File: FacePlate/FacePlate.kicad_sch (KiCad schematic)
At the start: 36 parts, among them J1 Conn_01x02_Pin, J2 GPIO, J3 Conn_01x04_Pin, J4 Conn_01x02_Pin, U7 AMS1117-3.3

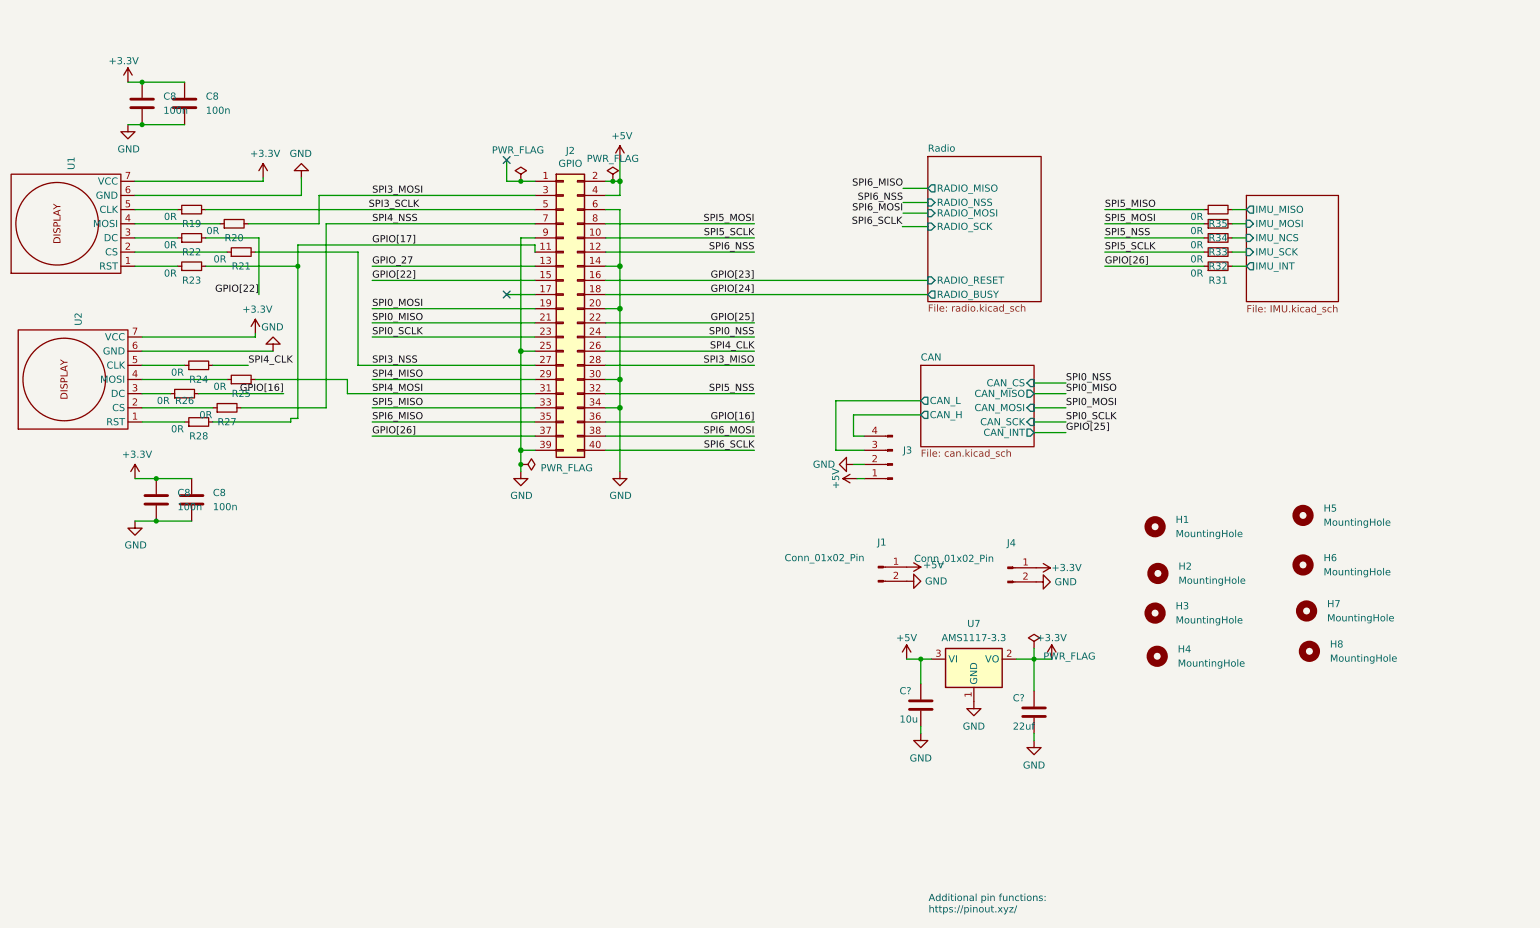
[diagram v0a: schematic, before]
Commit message: changed transceiver for faceplate
+ removed caps on chicker can
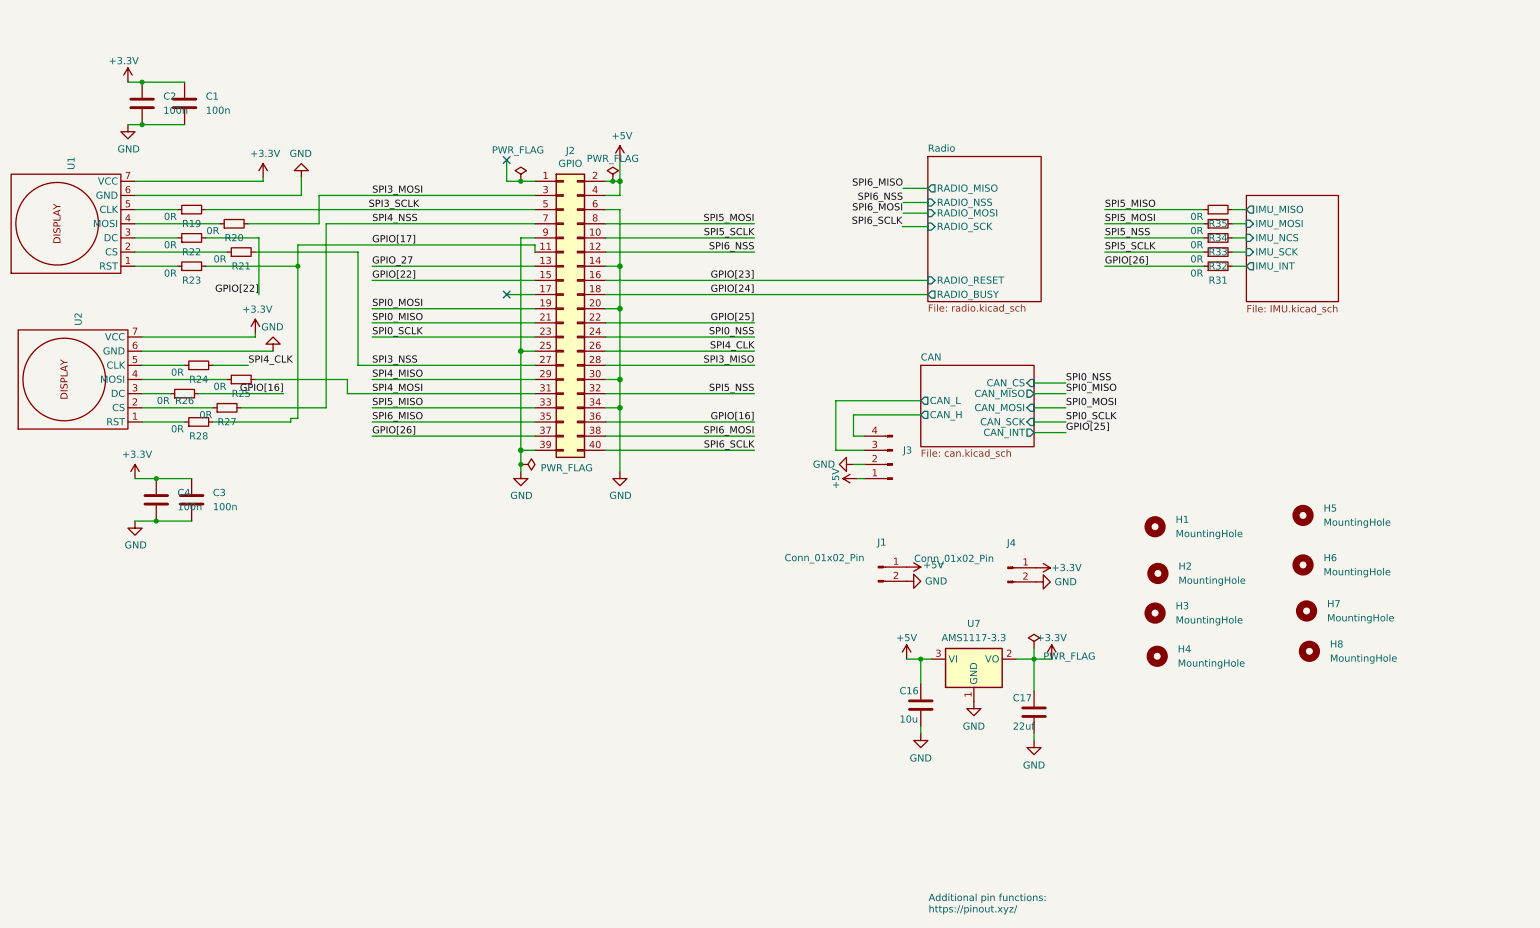
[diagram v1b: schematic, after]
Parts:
- gave numbers to parts that had none: 2
- renumbered C8 to C1, C8 to C2, C8 to C3, C8 to C4

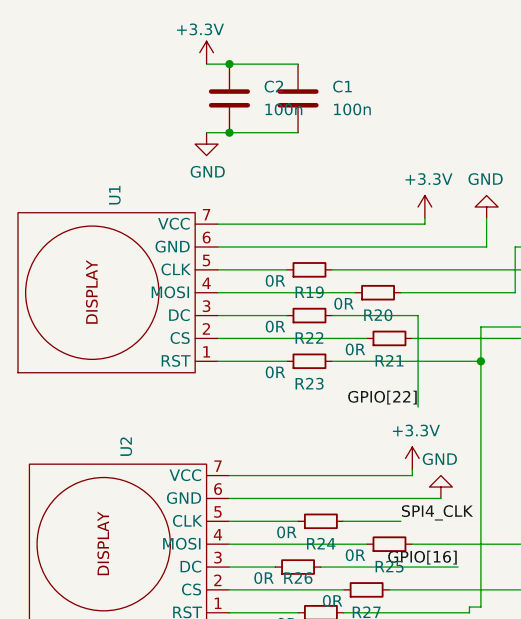
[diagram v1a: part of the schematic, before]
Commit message: faceplate. broken.
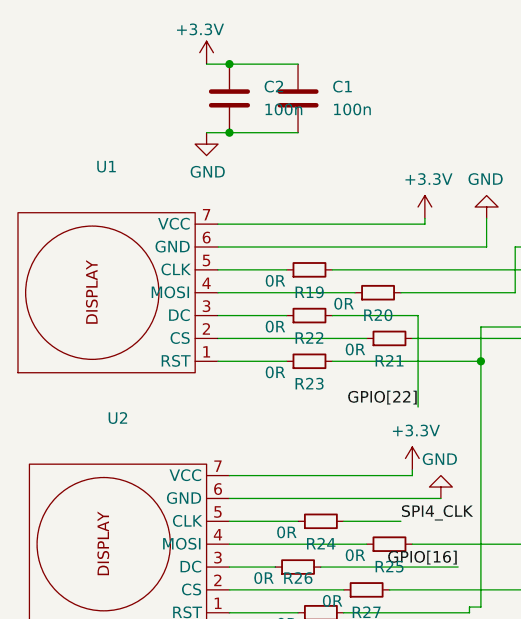
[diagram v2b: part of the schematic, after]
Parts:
- J2: footprint Connector_PinSocket_2.54mm:PinSocket_2x20_P2.54mm_Horizontal -> bots:PinSocket_2x20_P2.54mm_Horizontal; symbol Connector_Generic:Conn_02x20_Odd_Even -> bots:Conn_02x20_Odd_Even
- U1, U2: footprint Connector_PinSocket_2.54mm:PinSocket_1x07_P2.54mm_Vertical -> bots:GC9A_Display; symbol gc9a01:240_240_Round_Display -> bots:240_240_Round_Display
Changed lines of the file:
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@@
 	)
 	(symbol
-		(lib_id "Connector_Generic:Conn_02x20_Odd_Even")
+		(lib_id "bots:Conn_02x20_Odd_Even")
 		(at 113.665 71.12 0)
 		(unit 1)
@@
 			)
 		)
-		(property "Footprint" "Connector_PinSocket_2.54mm:PinSocket_2x20_P2.54mm_Horizontal"
-			(at -9.525 95.25 0)
+		(property "Footprint" "bots:PinSocket_2x20_P2.54mm_Horizontal"
+			(at 113.665 71.12 0)
 			(effects
 				(font
@@
 		)
 		(property "Datasheet" "~"
-			(at -9.525 95.25 0)
+			(at 113.665 71.12 0)
 			(effects
 				(font
@@
 			)
 		)
-		(property "Description" ""
+		(property "Description" "Generic connector, double row, 02x20, odd/even pin numbering scheme (row 1 odd numbers, row 2 even numbers), script generated (kicad-library-utils/schlib/autogen/connector/)"
 			(at 113.665 71.12 0)
 			(effects
@@
 					(size 1.27 1.27)
 				)
+				(hide yes)
 			)
 		)
@@
 	)
 	(symbol
-		(lib_id "gc9a01:240_240_Round_Display")
+		(lib_id "bots:240_240_Round_Display")
 		(at 12.7 83.82 90)
 		(unit 1)
@@
 		(fields_autoplaced yes)
 		(property "Reference" "U2"
-			(at 26.67 74.168 0)
+			(at 25.7175 69.85 90)
 			(effects
 				(font
 					(size 1.27 1.27)
 				)
-				(justify left)
 			)
 		)
 		(property "Value" "~"
-			(at 12.7 83.82 0)
+			(at 25.7175 72.39 90)
 			(effects
 				(font
@@
 			)
 		)
-		(property "Footprint" "Connector_PinSocket_2.54mm:PinSocket_1x07_P2.54mm_Vertical"
+		(property "Footprint" "bots:GC9A_Display"
 			(at 12.7 83.82 0)
 			(effects
@@
 					(size 1.27 1.27)
 				)
+				(hide yes)
 			)
 		)
@@
 	)
 	(symbol
-		(lib_id "gc9a01:240_240_Round_Display")
+		(lib_id "bots:240_240_Round_Display")
 		(at 11.43 55.88 90)
 		(unit 1)
@@
 		(fields_autoplaced yes)
 		(property "Reference" "U1"
-			(at 25.4 46.228 0)
+			(at 24.4475 41.91 90)
 			(effects
 				(font
 					(size 1.27 1.27)
 				)
-				(justify left)
 			)
 		)
 		(property "Value" "~"
-			(at 11.43 55.88 0)
+			(at 24.4475 44.45 90)
 			(effects
 				(font
@@
 			)
 		)
-		(property "Footprint" "Connector_PinSocket_2.54mm:PinSocket_1x07_P2.54mm_Vertical"
+		(property "Footprint" "bots:GC9A_Display"
 			(at 11.43 55.88 0)
 			(effects
@@
 					(size 1.27 1.27)
 				)
+				(hide yes)
 			)
 		)

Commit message: faceplate global files working
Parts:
- C16: footprint bots:C_0603_1608Metric -> bots:C_0805_2012Metric; symbol Device:C -> bots:C_10u; JLC (none) -> 0805; JLC Extended (none) -> no; LCSC C96446 -> C440198; MPN (none) -> GRM21BR61H106KE43L; Manufacturer (none) -> Murata; Price (none) -> 0.0645
- J3: symbol Connector:Conn_01x04_Pin -> bots:JST_XH_A_1x4
- R19, R20, R21, R22, R23, R24, R25, R26, R27, R28, R31, R32, R33, R34, R35: symbol bots:0R -> bots:R_0R; JLC (none) -> 0603; JLC Extended (none) -> no; MPN (none) -> 0603WAF0000T5E; Manufacturer (none) -> UNI-ROYAL(Uniroyal Elec); Price (none) -> 0.001
- U7: footprint Package_TO_SOT_SMD:SOT-223-3_TabPin2 -> bots:SOT-223-3_TabPin2; symbol Regulator_Linear:AMS1117-3.3 -> bots:AMS1117-3.3; JLC (none) -> SOT-223; JLC Extended (none) -> no; MPN (none) -> AMS1117-3.3; Manufacturer (none) -> Advanced Monolithic Systems; Price (none) -> 0.179
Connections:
- net GPIO[26]: no longer R31.1
- net IMU/IMU_INT: no longer R31.2
- net IMU/IMU_MISO: no longer R35.2
- net IMU/IMU_MOSI: no longer R34.2
- net IMU/IMU_NCS: no longer R33.2
- net IMU/IMU_SCK: no longer R32.2
- net SPI5_MISO: no longer R35.1
- net SPI5_MOSI: no longer R34.1
- net SPI5_NSS: no longer R33.1
- net SPI5_SCLK: no longer R32.1
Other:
- moved on the sheet: C16, C17, R19, R20, R22, R23, R24, R25, R27, R28

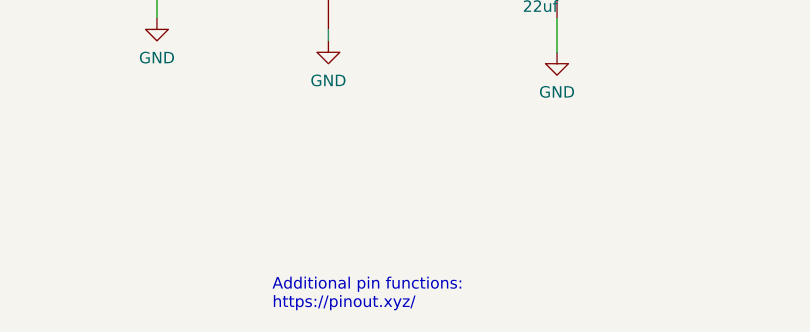
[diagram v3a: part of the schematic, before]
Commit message: added a title block
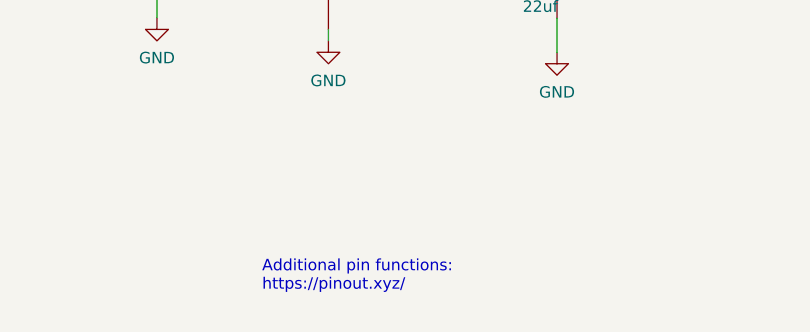
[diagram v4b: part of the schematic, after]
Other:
- company: (none) -> The Bots
- title: (none) -> Faceplate
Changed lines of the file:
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@@
 	(paper "A4")
 	(title_block
-		(date "15 nov 2012")
+		(title "Faceplate")
+		(date "2024-02-04")
+		(rev "V1.0")
+		(company "The Bots")
 	)
 	(text "Additional pin functions:\nhttps://pinout.xyz/"
 		(exclude_from_sim no)
-		(at 179.197 179.832 0)
+		(at 178.054 177.8 0)
 		(effects
 			(font

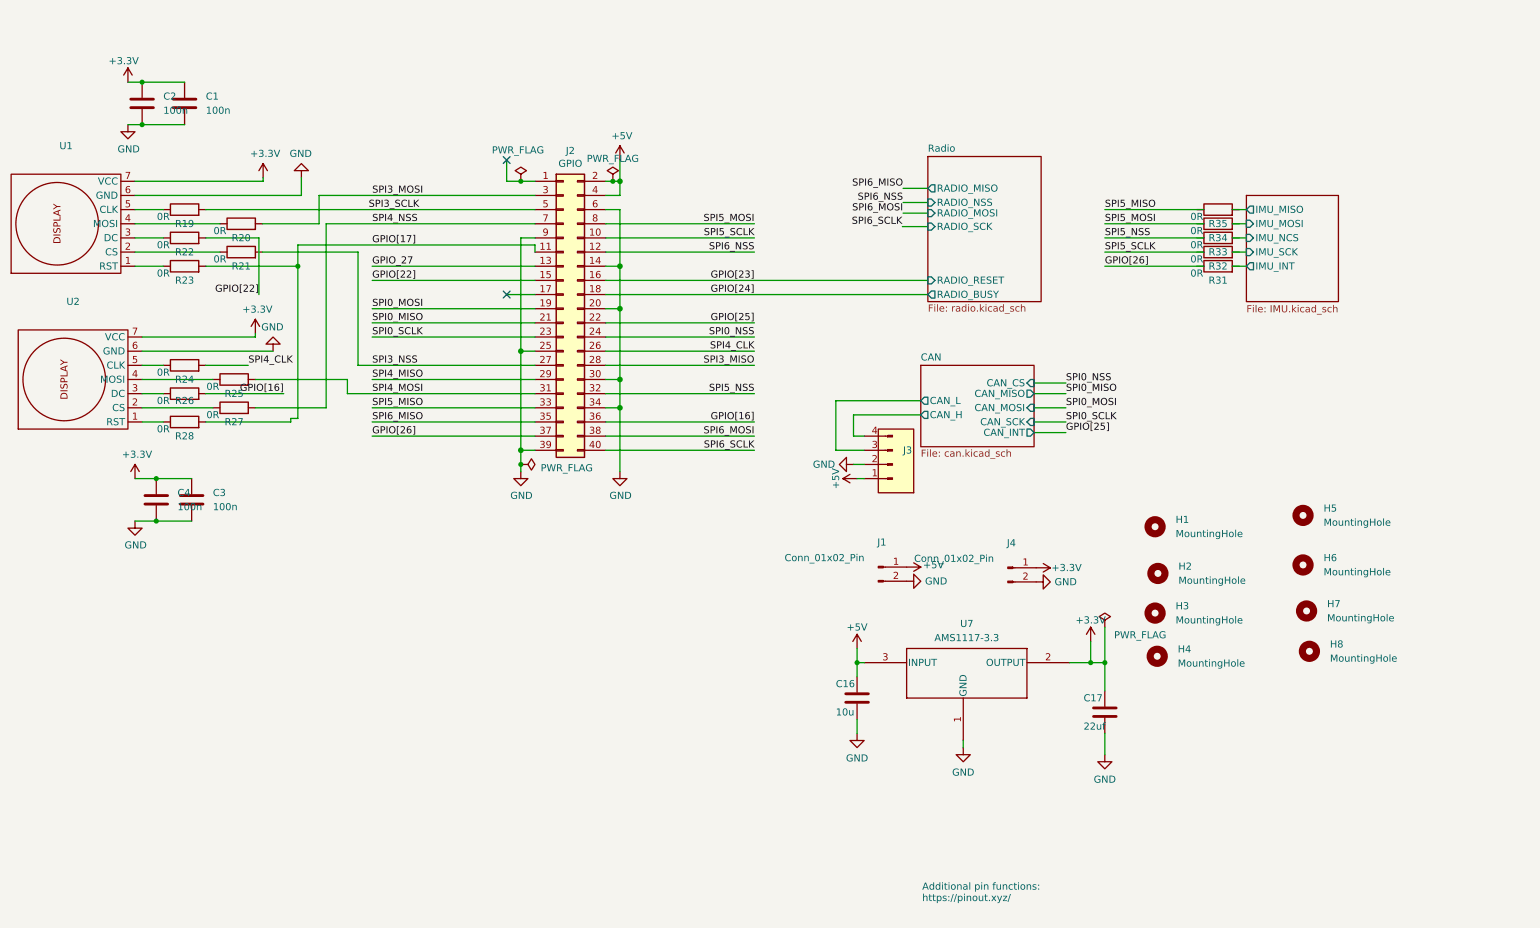
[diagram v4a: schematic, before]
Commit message: wip faceplate 2.0 schematic
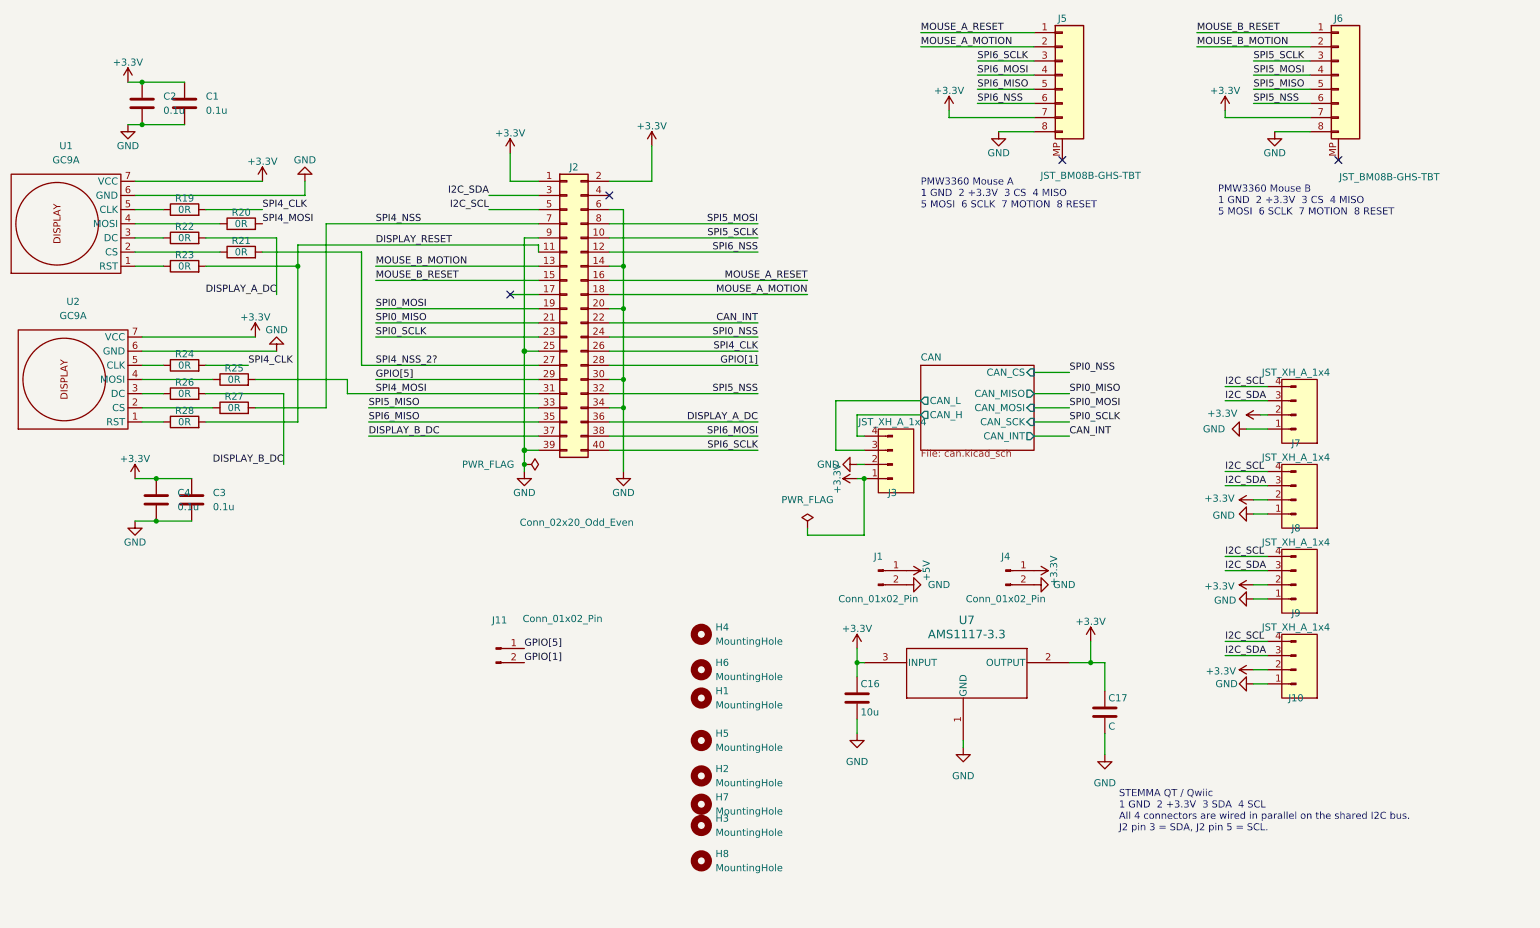
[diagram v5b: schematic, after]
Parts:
- removed R31, R32, R33, R34, R35: 0R, bots:R_0603_1608Metric, symbol bots:R_0R
- added J10, J7, J8, J9: JST_XH_A_1x4, bots:JST_XH_B4B-XH-AM_1x04_P2.50mm_Vertical, symbol bots:JST_XH_A_1x4
- added J11: Conn_01x02_Pin, symbol Connector:Conn_01x02_Pin
- added J5, J6: JST_BM08B-GHS-TBT, bots:JST_BM08B-GHS-TBT_LF__SN__N_, symbol bots:JST_BM08B-GHS-TBT
- C1, C2, C3, C4: value 100n -> 0.1u; footprint bots:C_0402_1005Metric -> bots:C_0603_1608Metric; JLC (none) -> 0603; JLC Extended (none) -> no; LCSC C307331 -> C14663; MPN (none) -> CC0603KRX7R9BB104; Manufacturer (none) -> YAGEO; Price (none) -> 0.0021
- C17: value 22uf -> C; footprint bots:C_0603_1608Metric -> (none); LCSC C59461 -> (none)
- H1, H2, H3, H4, H5, H6, H7, H8: footprint MountingHole:MountingHole_2.7mm_M2.5 -> (none); now left out of the parts list
- J1, J4: footprint Connector_PinHeader_2.54mm:PinHeader_1x02_P2.54mm_Vertical -> (none)
- J2: value GPIO -> Conn_02x20_Odd_Even; footprint bots:PinSocket_2x20_P2.54mm_Horizontal -> Connector_PinSocket_2.54mm:PinSocket_2x20_P2.54mm_Horizontal
- J3: value Conn_01x04_Pin -> JST_XH_A_1x4; footprint Connector_JST:JST_XH_B4B-XH-AM_1x04_P2.50mm_Vertical -> bots:JST_XH_B4B-XH-AM_1x04_P2.50mm_Vertical
- U1, U2: value ~ -> GC9A; LCSC C718238 -> (none)
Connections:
- net +3.3V: now also C16.1, J2.1 (Pin_1), J2.2 (Pin_2), J3.1 (Pin_1), U7.3 (INPUT), J10.2 (Pin_2), J5.7 (Pin_7), J6.7 (Pin_7), J7.2 (Pin_2), J8.2 (Pin_2), J9.2 (Pin_2)
- net +5V: no longer C16.1, J2.2 (Pin_2), J2.4 (Pin_4), J3.1 (Pin_1), U7.3 (INPUT)
- net GND: now also J10.1 (Pin_1), J5.8 (Pin_8), J6.8 (Pin_8), J7.1 (Pin_1), J8.1 (Pin_1), J9.1 (Pin_1)
- net SPI4_CLK: now also R19.2
- net SPI4_MOSI: now also R20.2
- net SPI5_MISO: now also J6.5 (Pin_5)
- net SPI5_MOSI: now also J6.4 (Pin_4)
- net SPI5_NSS: now also J6.6 (Pin_6)
- net SPI5_SCLK: now also J6.3 (Pin_3)
- net SPI6_MISO: now also J5.5 (Pin_5)
- net SPI6_MOSI: now also J5.4 (Pin_4)
- net SPI6_NSS: now also J5.6 (Pin_6)
- net SPI6_SCLK: now also J5.3 (Pin_3)
- net GPIO[16] renamed DISPLAY_A_DC
- net DISPLAY_A_DC: now also R22.2; no longer R26.2
- net GPIO[17] renamed DISPLAY_RESET
- net GPIO[22] renamed MOUSE_B_RESET
- net MOUSE_B_RESET: now also J6.1 (Pin_1); no longer R22.2
- net GPIO[23] renamed MOUSE_A_RESET
- net MOUSE_A_RESET: now also J5.1 (Pin_1)
- net GPIO[24] renamed MOUSE_A_MOTION
- net MOUSE_A_MOTION: now also J5.2 (Pin_2)
- net GPIO[25] renamed CAN_INT
- net GPIO[26] renamed DISPLAY_B_DC
- net DISPLAY_B_DC: now also R26.2
- net GPIO_27 renamed MOUSE_B_MOTION
- net MOUSE_B_MOTION: now also J6.2 (Pin_2)
- net SPI3_MISO renamed GPIO[1]
- net GPIO[1]: now also J11.2 (Pin_2)
- net SPI3_MOSI renamed I2C_SDA
- net I2C_SDA: now also J10.3 (Pin_3), J7.3 (Pin_3), J8.3 (Pin_3), J9.3 (Pin_3); no longer R20.2
- net SPI3_NSS renamed SPI4_NSS_2?
- net SPI3_SCLK renamed I2C_SCL
- net I2C_SCL: now also J10.4 (Pin_4), J7.4 (Pin_4), J8.4 (Pin_4), J9.4 (Pin_4); no longer R19.2
- net SPI4_MISO renamed GPIO[5]
- net GPIO[5]: now also J11.1 (Pin_1)
- no-connect marks 2 -> 4
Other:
- removed sheet IMU
- removed sheet Radio
- note added: "PMW3360 Mouse A 1 GND 2 +3.3V 3 CS 4 MISO 5 MOSI 6 SCLK 7 MOTION 8 RESET"
- note added: "PMW3360 Mouse B 1 GND 2 +3.3V 3 CS 4 MISO 5 MOSI 6 SCLK 7 MOTION 8 RESET"
- note added: "STEMMA QT / Qwiic 1 GND 2 +3.3V 3 SDA 4 SCL All 4 connectors are wired in parallel on the shared I2C bus. J2 pin 3 = SDA, J2 pin 5 = SCL."
- note removed: "Additional pin functions: https://pinout.xyz/"
- moved on the sheet: H1, H2, H3, H4, H5, H6, H7, H8, J1, J4

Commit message: wip some more
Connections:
- net +3.3V: no longer C16.1, J2.1 (Pin_1), J2.2 (Pin_2), J3.1 (Pin_1), U7.3 (INPUT)
- net +5V: now also C16.1, J2.2 (Pin_2), J2.4 (Pin_4), J3.1 (Pin_1), U7.3 (INPUT)
